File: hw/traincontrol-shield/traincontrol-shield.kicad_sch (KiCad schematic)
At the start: 3 parts, among them J4 Track Input, J5 Motor Windings, J6 Motor+AC

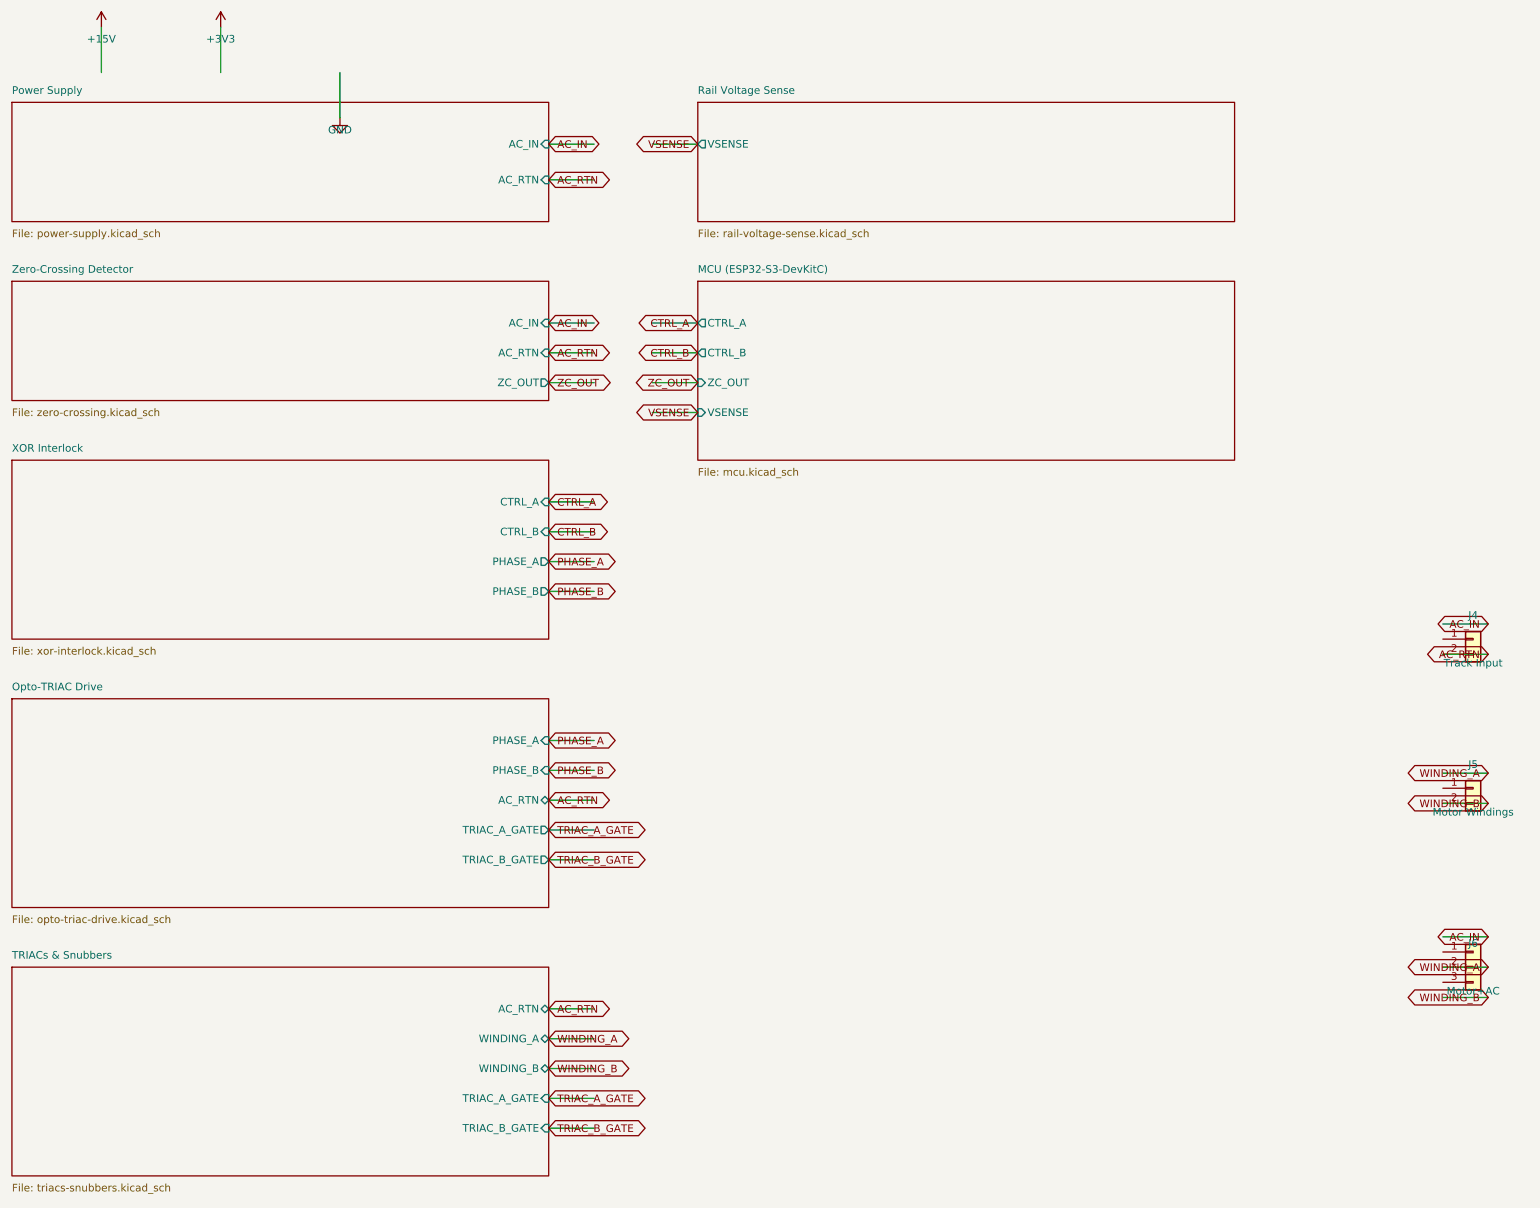
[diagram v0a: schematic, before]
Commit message: Fix duplicate #PWR refs, top-level label placement, and sheet box width
- #PWR references: assign unique page×100 offset per sheet (201..801 + 101
  for top-level) and standardise to #PWR{n:04d} format — eliminates duplicate
  reference designators across the project
- Top-level glabel: place label (at x ...) in the inter-column gap rather than
  (at lx ...) at the sheet border; wire already spans border→gap correctly;
  no more floating wire endpoints or label body overlapping sheet-box pins
- BOX_W: 90→65 mm, LX: 130→110 mm (gap 30 mm, label clearance 14.76 mm);
  connector J4/J5/J6 x: 260→190 mm to match new right-column right border
- All 8 sheets regenerated and validated with kicad-cli

Co-Authored-By: Claude Sonnet 4.6 <noreply@anthropic.com>
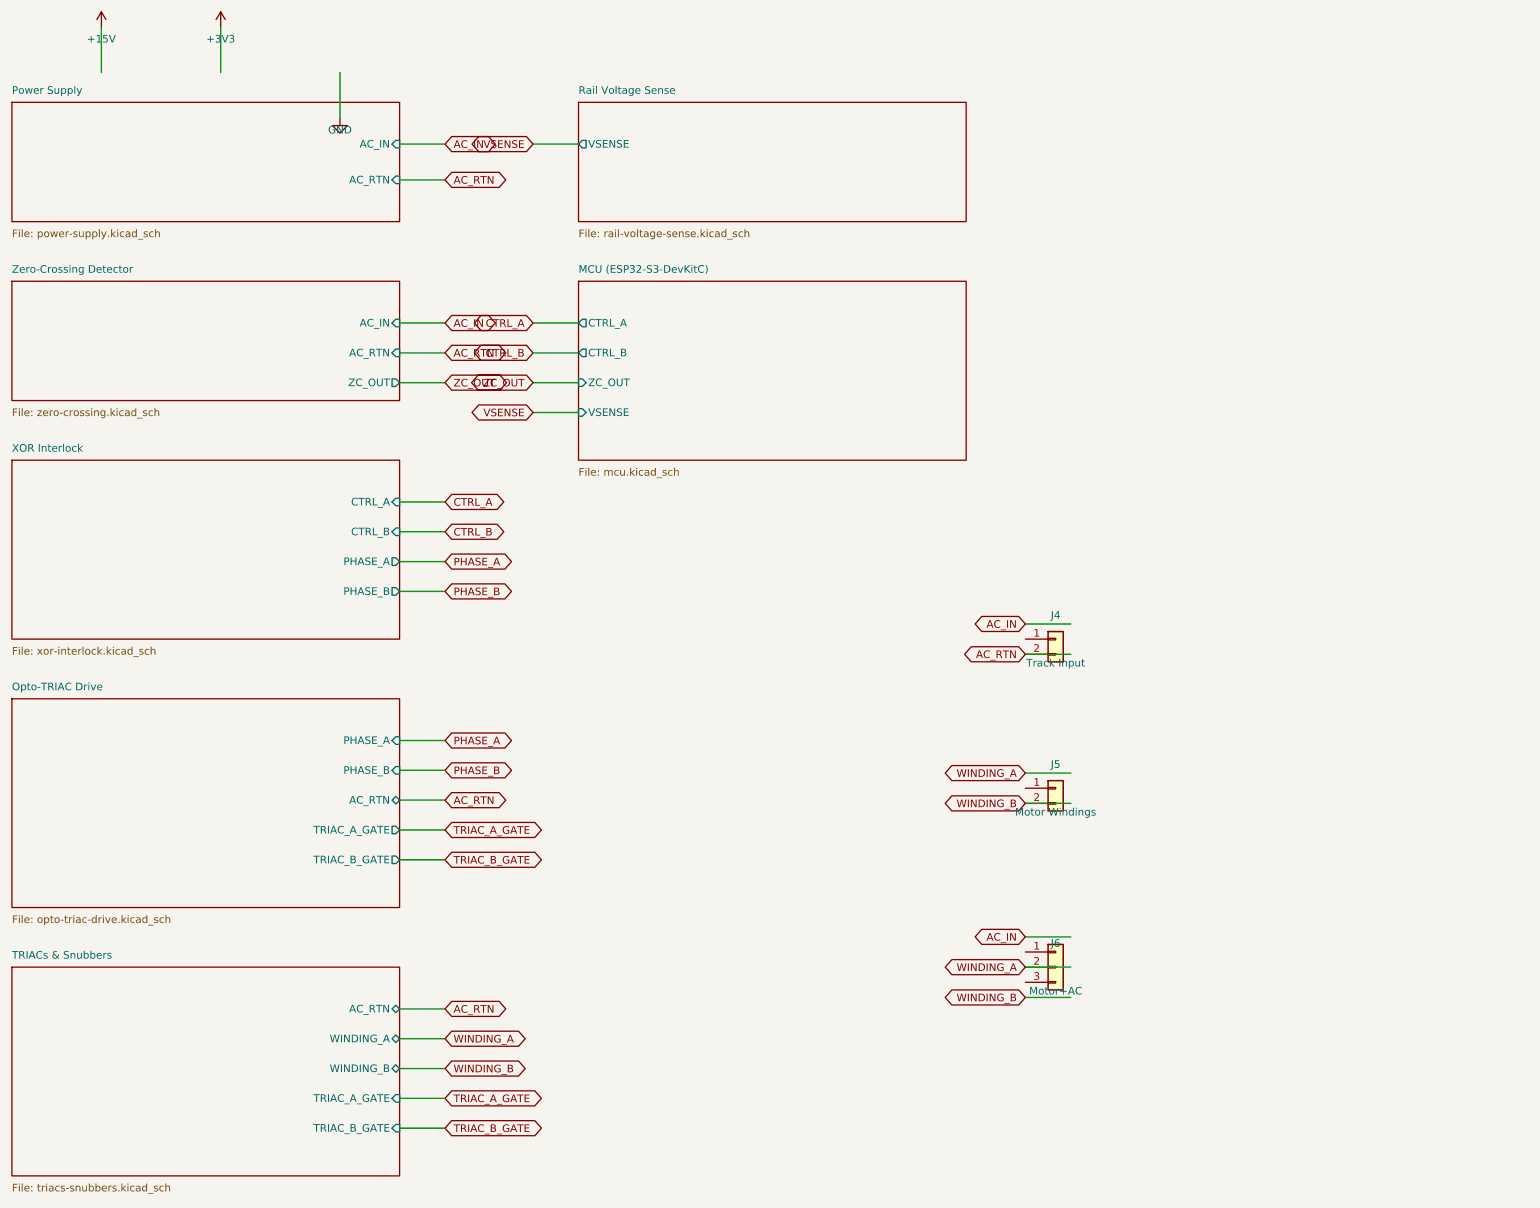
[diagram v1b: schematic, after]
